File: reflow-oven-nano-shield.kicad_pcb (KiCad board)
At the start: 2 copper layers, 92.7 x 59.7 mm, 41 parts, among them J1 POWER IN, J2 SSR OUT, J3 SERVO, Q1 2N3904, Q2 2N3904, Q3 2N3904, Q4 2N3904, Q5 2N3904, SW1 TOP, SW2 BOTTOM

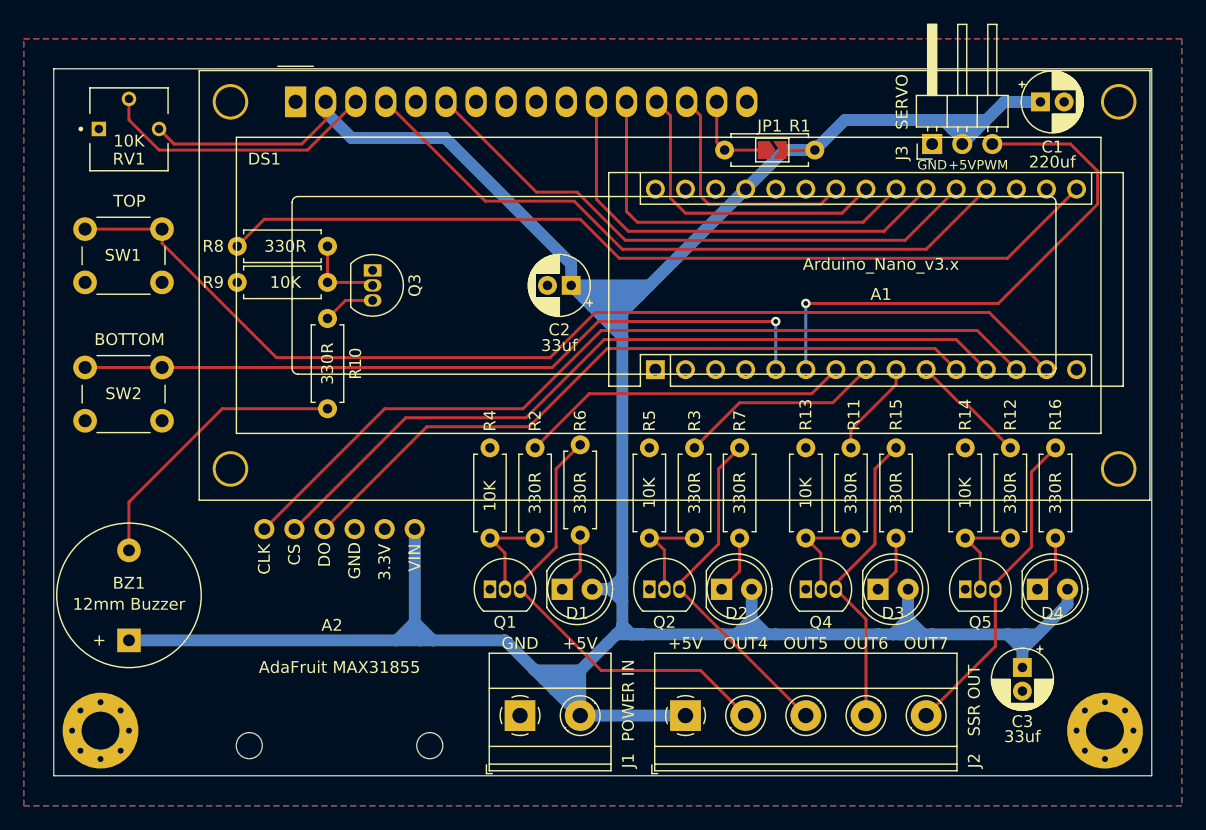
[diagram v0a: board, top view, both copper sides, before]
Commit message: Hand solder TO-92 footprint, add teardrops
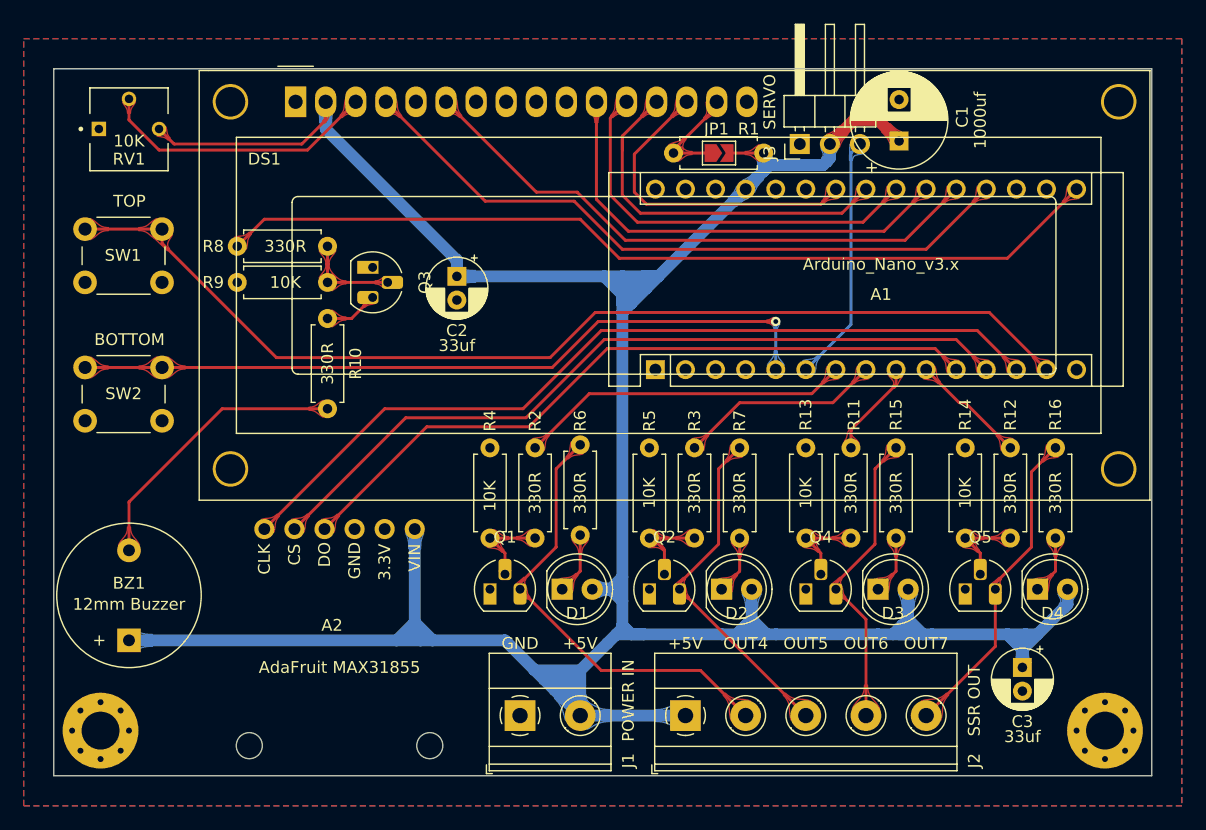
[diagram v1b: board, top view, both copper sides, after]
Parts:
- C1: value 220uf -> 1000uf; footprint Capacitor_THT:CP_Radial_D5.0mm_P2.00mm -> Capacitor_THT:CP_Radial_D8.0mm_P3.50mm
- Q1, Q2, Q3, Q4, Q5: footprint Package_TO_SOT_THT:TO-92_Inline -> Package_TO_SOT_THT:TO-92_HandSolder
- moved C1 12.4 mm to (160.3, 49.3), turned to 90 degrees
- moved J3 11.2 mm to (151.9, 49.5)
- moved C2 9.68 mm to (122.9, 60.7), turned to 270 degrees
- moved JP1 4.51 mm to (145.1, 50.3)
- moved R1 4.33 mm to (148.8, 50.3)
- moved Q3 0.25 mm to (115.8, 59.9)
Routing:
- net /D3_SERVO: track 46.3 -> 20.9 mm, vias 1 -> 0
- net +5V: track 304.4 -> 290.0 mm
- net /A5_DATA3: track 20.7 -> 27.4 mm
- net /A4_DATA2: track 26.5 -> 32.3 mm
- net Net-(Q4-Pad2): track 8.65 -> 7.38 mm
- net Net-(Q5-Pad2): track 8.65 -> 7.38 mm
- net Net-(Q2-Pad2): track 8.80 -> 7.53 mm
- net Net-(Q1-Pad2): track 8.65 -> 7.38 mm
- net Net-(DS1-Pad15): track 7.65 -> 8.89 mm
- net Net-(Q3-Pad2): track 6.96 -> 8.13 mm
- net /A3_DATA1: track 33.5 -> 34.7 mm
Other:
- board text added: "JLCJLCJLCJLC"
- board text added: "Reflow Oven Nano Shield v1.0 PCB by Chris Tersteeg github.com/djtersteegc/reflow-oven-nano-shield ControlLeo2 Software by Peter Easton github.com/engineertype/ControLeo2"
